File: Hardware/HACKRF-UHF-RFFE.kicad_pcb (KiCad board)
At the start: 4 copper layers, 84 parts, among them J1 SMA_Wurth_60312242114510, J2 SMA_Wurth_60312242114510, J3 SMA_Wurth_60312242114510, K1 HF3-53, Q1 SSM3K15AFU, U1 SPF5189Z, U2 RFPA3800, U3 SPF5189Z, U4 AS169-73, U5 SPF5189Z, U6 AS169-73, U7 AS169-73

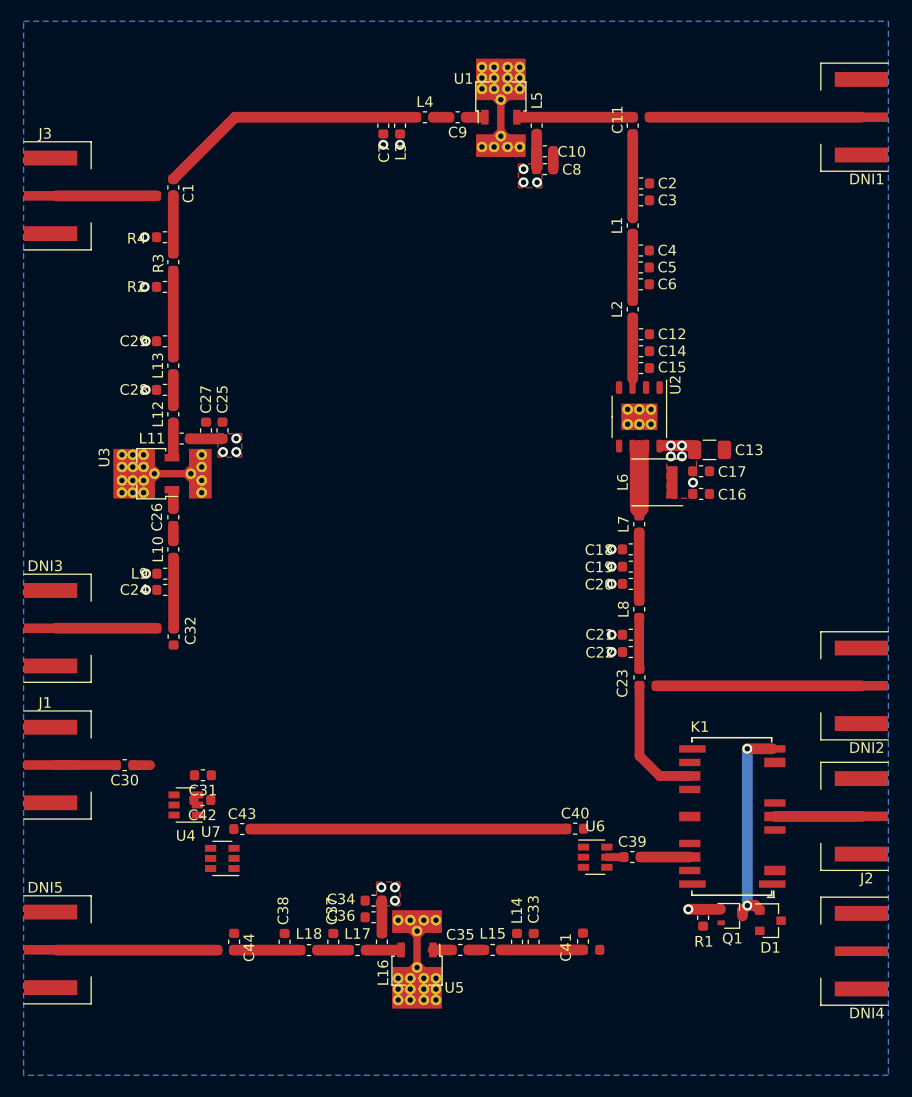
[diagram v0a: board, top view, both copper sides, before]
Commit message: Added discrete Chebyshev input filter to schematic based on Qucs simulationd. Artwork not done. It has occurred to me that I need to do some major cleanup of the test points on this PCBA.
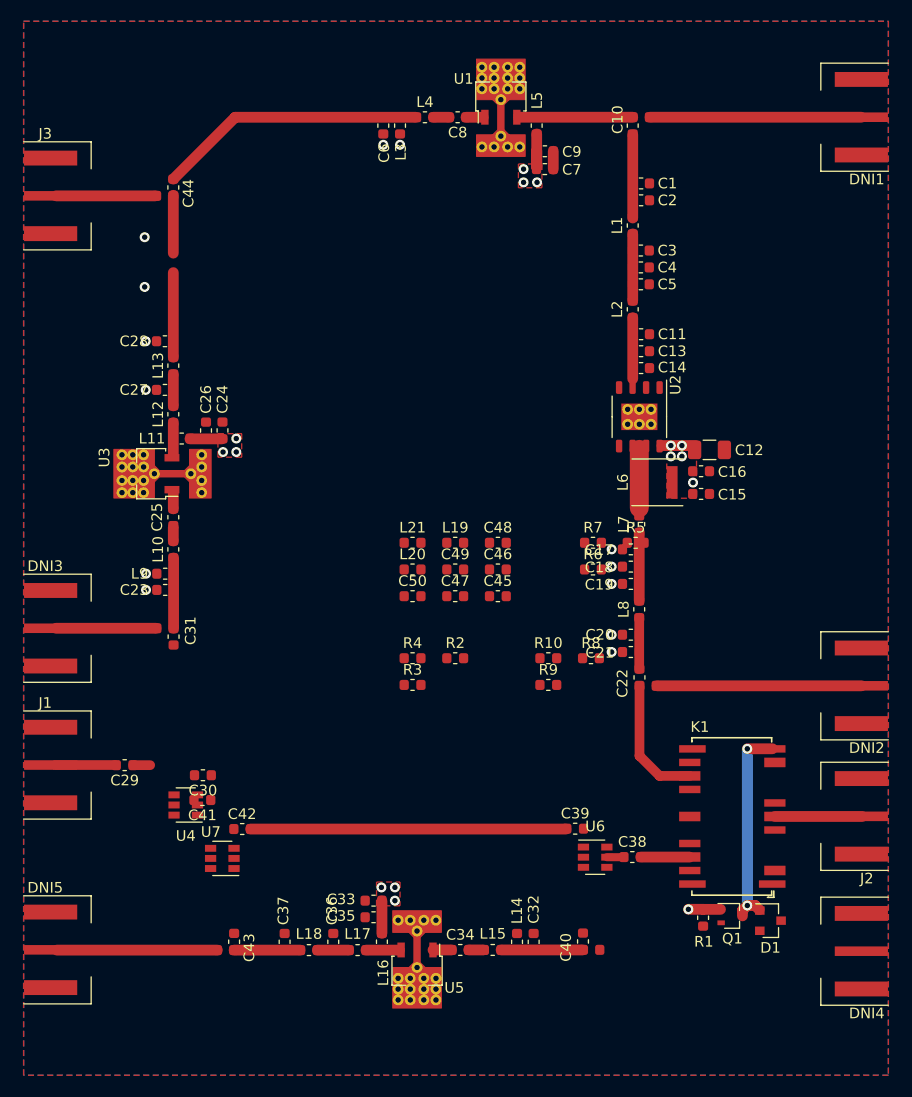
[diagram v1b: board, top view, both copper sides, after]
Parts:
- added C45: 600S100, Capacitor_SMD:C_0603_1608Metric, F.Cu at (143.6, 112.5)
- added C46: 600S220, Capacitor_SMD:C_0603_1608Metric, F.Cu at (143.6, 109.9)
- added C47: 600S2R7, Capacitor_SMD:C_0603_1608Metric, F.Cu at (139.6, 112.5)
- added C48: 600S2R7, Capacitor_SMD:C_0603_1608Metric, F.Cu at (143.6, 107.4)
- added C49: 600S220, Capacitor_SMD:C_0603_1608Metric, F.Cu at (139.6, 109.9)
- added C50: 600S100, Capacitor_SMD:C_0603_1608Metric, F.Cu at (135.6, 112.5)
- added L19: 0603HP-3N6X, Inductor_SMD:L_0603_1608Metric, F.Cu at (139.6, 107.4)
- added L20: 0603HP-82NX, Inductor_SMD:L_0603_1608Metric, F.Cu at (135.6, 109.9)
- added L21: 0603HP-3N6X, Inductor_SMD:L_0603_1608Metric, F.Cu at (135.6, 107.4)
- added R10: RT0603DRE0796R5L, Resistor_SMD:R_0603_1608Metric, F.Cu at (148.4, 118.3)
- added R5: RT0603DRE0796R5L, Resistor_SMD:R_0603_1608Metric, F.Cu at (156.6, 107.4)
- added R6: RT0603BRD0771R5L, Resistor_SMD:R_0603_1608Metric, F.Cu at (152.6, 109.9)
- added R7: RT0603DRE0796R5L, Resistor_SMD:R_0603_1608Metric, F.Cu at (152.6, 107.4)
- added R8: RT0603DRE0796R5L, Resistor_SMD:R_0603_1608Metric, F.Cu at (152.4, 118.3)
- added R9: RT0603BRD0771R5L, Resistor_SMD:R_0603_1608Metric, F.Cu at (148.4, 120.8)
- moved R4 45.9 mm to (135.6, 118.3), turned to 0 degrees
- moved R3 45.7 mm to (135.6, 120.8), turned to 0 degrees
- moved R2 44.3 mm to (139.6, 118.3), turned to 0 degrees
- renumbered C2 to C1, C11 to C10, C12 to C11, C13 to C12, C14 to C13, C15 to C14, C16 to C15, C17 to C16, C18 to C17, C19 to C18, C20 to C19, C3 to C2, C21 to C20, C22 to C21, C23 to C22, C24 to C23, C25 to C24, C26 to C25, C27 to C26, C28 to C27, C29 to C28, C30 to C29, C4 to C3, C31 to C30, C32 to C31, C33 to C32, C34 to C33, C35 to C34, C36 to C35, C37 to C36, C38 to C37, C39 to C38, C40 to C39, C5 to C4, C41 to C40, C42 to C41, C43 to C42, C44 to C43, C1 to C44, C6 to C5, C7 to C6, C8 to C7, C9 to C8, C10 to C9
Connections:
- J1 pad 1: /sheet5F20A948/J1 -> /Sheet5F20B395/RF_IN
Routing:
- added copper zone on F.Cu, net GNDA

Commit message: Major cleanup to both the schematic and directory structure. Stackup has changed accomodate to 0.65mm trace width. Chebyshev filter lived through the experience in the Qucs simulation; others not checked yet. I do want to re-visit the matching networks of all of the amplifiers as I have developed some good strategies to implement them.
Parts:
- removed J3: SMA_Wurth_60312242114510, RF:SMA_Wurth_60312242114510
- added C51: 600S101_3-pad-R, Capacitor_SMD:C_0603_1608Metric_3-pad-R, F.Cu at (-156.7, -74.0)
- added DNI6: SMA_Wurth_60312242114510, RF:SMA_Wurth_60312242114510, F.Cu at (-163.9, -69.6)
- C1: value 600S1R5 -> 600S101
- C10: value 600S101_3-pad-R -> 600S101; footprint Capacitor_SMD:C_0603_1608Metric_3-pad-R -> Capacitor_SMD:C_0603_1608Metric
- C11: value 600S3R3 -> 600S101
- C12: value T491A106M016AH -> 600S101_3-pad-L; footprint Capacitor_SMD:C_1206_3216Metric -> Capacitor_SMD:C_0603_1608Metric_3-pad-L
- C13, C2: value 600S100 -> 600S101
- C14: value 600S120 -> 600S101
- C15: value CC0603KRX7R9BB104 -> 600S101_3-pad-R; footprint Capacitor_SMD:C_0603_1608Metric -> Capacitor_SMD:C_0603_1608Metric_3-pad-R
- C16: value 600S101 -> 600S100; footprint Resistor_SMD:R_0603_1608Metric -> Capacitor_SMD:C_0603_1608Metric
- C17: value 600S270 -> 600S220
- C18: value 600S100 -> 600S2R7
- C19: value 600S3R6 -> 600S2R7
- C20: value 600S100 -> 600S220
- C21, C34: value 600S2R2 -> 600S100
- C22: value 600S101_3-pad-L -> 600S101; footprint Capacitor_SMD:C_0603_1608Metric_3-pad-L -> Capacitor_SMD:C_0603_1608Metric
- C23: value 600S120 -> 600S1R5
- C24: value CC0603KRX7R9BB104 -> 600S100
- C25: value 600S2R2 -> 600S3R0
- C26, C39, C41: value 600S101 -> 600S100
- C27: value 600S6R2 -> 600S270
- C28: value 600S5R1 -> 600S120; footprint Capacitor_SMD:C_0603_1608Metric -> Resistor_SMD:R_0603_1608Metric
- C29: value 600S101 -> CC0603KRX7R9BB104
- C3: value 600S3R0 -> 600S101_3-pad-L; footprint Capacitor_SMD:C_0603_1608Metric -> Capacitor_SMD:C_0603_1608Metric_3-pad-L
- C30: value 600S101 -> 600S2R2; footprint Capacitor_SMD:C_0603_1608Metric -> Resistor_SMD:R_0603_1608Metric
- C31: value 600S101_3-pad-L -> 600S101; footprint Capacitor_SMD:C_0603_1608Metric_3-pad-L -> Resistor_SMD:R_0603_1608Metric
- C32: value 600S120 -> 600S3R3
- C33: value CC0603KRX7R9BB104 -> T491A106M016AH; footprint Capacitor_SMD:C_0603_1608Metric -> Capacitor_SMD:C_1206_3216Metric
- C35: value 600S101 -> 600S120
- C36: value 600S6R2 -> CC0603KRX7R9BB104
- C37: value 600S5R1 -> 600S101; footprint Capacitor_SMD:C_0603_1608Metric -> Resistor_SMD:R_0603_1608Metric
- C38: value 600S101 -> 600S270
- C4, C45: value 600S100 -> 600S120
- C40: value 600S101_3-pad-L -> 600S3R6; footprint Capacitor_SMD:C_0603_1608Metric_3-pad-L -> Capacitor_SMD:C_0603_1608Metric
- C42: value 600S101 -> 600S2R2
- C44: value 600S101_3-pad-R -> 600S101_3-pad-L; footprint Capacitor_SMD:C_0603_1608Metric_3-pad-R -> Capacitor_SMD:C_0603_1608Metric_3-pad-L
- C46: value 600S220 -> CC0603KRX7R9BB104
- C47: value 600S2R7 -> 600S2R2
- C48: value 600S2R7 -> 600S101
- C49: value 600S220 -> 600S6R2
- C5: value 600S270 -> CC0603KRX7R9BB104
- C50: value 600S100 -> 600S5R1
- C6: value 600S120 -> 600S2R2; footprint Resistor_SMD:R_0603_1608Metric -> Capacitor_SMD:C_0603_1608Metric
- C7: value CC0603KRX7R9BB104 -> 600S101
- C8: value 600S2R2 -> 600S6R2; footprint Resistor_SMD:R_0603_1608Metric -> Capacitor_SMD:C_0603_1608Metric
- C9: value 600S101 -> 600S5R1; footprint Resistor_SMD:R_0603_1608Metric -> Capacitor_SMD:C_0603_1608Metric
- L1: footprint Inductor_SMD:L_0603_1608Metric -> Resistor_SMD:R_0603_1608Metric
- L10, L15: value 0603HP-51NX -> 0603HP-1N8X; footprint Resistor_SMD:R_0603_1608Metric -> Inductor_SMD:L_0603_1608Metric
- L11: value 0603HP-R22X -> 0603HP-8N2X
- L12: value 0603HP-3N6X -> 0603HP-51NX
- L13: value 0603HP-15NX -> 0603HP-R22X
- L14: value 0603HP-8N2X -> 1111SQ-47N; footprint Resistor_SMD:R_0603_1608Metric -> Inductor_SMD:L_Coilcraft_1111SQ-47N
- L16: value 0603HP-R22X -> 0603HP-8N2X; footprint Resistor_SMD:R_0603_1608Metric -> Inductor_SMD:L_0603_1608Metric
- L17: value 0603HP-3N6X -> 0603HP-8N2X
- L18: value 0603HP-15NX -> 0603HP-51NX
- L19: value 0603HP-3N6X -> 0603HP-R22X; footprint Inductor_SMD:L_0603_1608Metric -> Resistor_SMD:R_0603_1608Metric
- L2: value 0603HP-1N8X -> 0603HP-51NX; footprint Inductor_SMD:L_0603_1608Metric -> Resistor_SMD:R_0603_1608Metric
- L20: value 0603HP-82NX -> 0603HP-3N6X; footprint Inductor_SMD:L_0603_1608Metric -> Resistor_SMD:R_0603_1608Metric
- L21: value 0603HP-3N6X -> 0603HP-15NX; footprint Inductor_SMD:L_0603_1608Metric -> Resistor_SMD:R_0603_1608Metric
- L3: value 0603HP-8N2X -> 0603HP-R22X
- L4: value 0603HP-51NX -> 0603HP-3N6X
- L5: value 0603HP-R22X -> 0603HP-15NX
- L6: value 1111SQ-47N -> 0603HP-3N6X; footprint Inductor_SMD:L_Coilcraft_1111SQ-47N -> Inductor_SMD:L_0603_1608Metric
- L7: value 0603HP-1N8X -> 0603HP-82NX
- L8: value 0603HP-8N2X -> 0603HP-3N6X
- L9: footprint Resistor_SMD:R_0603_1608Metric -> Inductor_SMD:L_0603_1608Metric
- U1, U3: value SPF5189Z -> AS169-73; footprint RF:SOT-89-3_Qorvo_SPF5189z -> Package_TO_SOT_SMD:SOT-23-6
- U2: value RFPA3800 -> SPF5189Z; footprint RF:SOIC-8_Qorvo_RFPA3800 -> RF:SOT-89-3_Qorvo_SPF5189z
- U6: value AS169-73 -> RFPA3800; footprint Package_TO_SOT_SMD:SOT-23-6 -> RF:SOIC-8_Qorvo_RFPA3800
- U7: value AS169-73 -> SPF5189Z; footprint Package_TO_SOT_SMD:SOT-23-6 -> RF:SOT-89-3_Qorvo_SPF5189z
- moved D1 438.0 mm to (-202.8, -88.1)
- moved DNI4 437.3 mm to (-213.6, -49.3), turned to 0 degrees
- moved K1 433.7 mm to (-210.8, -82.1), turned to 0 degrees
- moved Q1 431.1 mm to (-198.3, -88.6)
- moved R1 430.8 mm to (-203.0, -84.6), turned to 0 degrees
- moved U6 418.4 mm to (-212.4, -67.2)
- moved C38 414.7 mm to (-208.6, -60.2)
- moved L14 414.0 mm to (-213.6, -61.1), turned to 0 degrees
- moved C40 412.6 mm to (-200.6, -69.2), turned to 0 degrees
- moved C39 405.9 mm to (-202.2, -65.9)
- moved C32 405.2 mm to (-200.6, -63.4), turned to 0 degrees
- moved C34 401.8 mm to (-204.6, -60.9)
- moved L8 400.6 mm to (-214.6, -36.1), turned to 0 degrees
- moved C18 399.3 mm to (-214.6, -38.6), turned to 0 degrees
- moved L15 399.3 mm to (-196.6, -64.1), turned to 0 degrees
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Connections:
- C1 pad 1: /Sheet5F04F5B5/PA_Driver/RF_OUT -> Net-(C1-Pad1)
- C1 pad 2: GNDA -> /sheet5F20A948/J1
- C10 pad 2: /Sheet5F04F5B5/PA_Driver/RF_OUT -> /sheet5F20DB04/J1
- C11 pad 1: /Sheet5F04F5B5/PA_Final/RF_IN -> /sheet5F2751CB/J2
- C11 pad 2: GNDA -> Net-(C11-Pad2)
- C12 pad 1: /Sheet5F04F5B5/P7V -> /sheet5F20DB04/J2
- C12 pad 2: GNDA -> /sheet5F20DB04/Sheet5F1AEEB0/DISCONNECT
- C13 pad 1: /Sheet5F04F5B5/PA_Final/RF_IN -> Net-(C13-Pad1)
- C13 pad 2: GNDA -> /sheet5F2751CB/J1
- C14 pad 1: /Sheet5F04F5B5/PA_Final/RF_IN -> /sheet5F2751CB/J2
- C14 pad 2: GNDA -> Net-(C14-Pad2)
- C15 pad 1: /Sheet5F04F5B5/P7V -> /sheet5F2751CB/J3
- C15 pad 2: GNDA -> /sheet5F2751CB/Sheet5F1B84EB/DISCONNECT
- C16 pad 1: /Sheet5F04F5B5/P7V -> /Sheet5F20B395/sheet5F216BC2/RF_IN
- C16 pad 2: GNDA -> GND
- C17 pad 1: Net-(C17-Pad1) -> /Sheet5F20B395/sheet5F216BC2/RF_IN
- C17 pad 2: GNDA -> GND
- C18 pad 1: Net-(C17-Pad1) -> Net-(C18-Pad1)
- C18 pad 2: GNDA -> /Sheet5F20B395/sheet5F216BC2/RF_IN
- C19 pad 1: Net-(C17-Pad1) -> Net-(C19-Pad1)
- C19 pad 2: GNDA -> /Sheet5F20B395/sheet5F20E71B/RF_IN
- C2 pad 1: /Sheet5F04F5B5/PA_Driver/RF_OUT -> /sheet5F2751CB/J1
- C2 pad 2: GNDA -> Net-(C2-Pad2)
- C20 pad 1: Net-(C20-Pad1) -> GND
- C20 pad 2: GNDA -> /Sheet5F20B395/sheet5F20E71B/RF_IN
- C21 pad 1: Net-(C20-Pad1) -> /Sheet5F20B395/sheet5F20E71B/RF_IN
- C21 pad 2: GNDA -> GND
- C22 pad 1: /Sheet5F04F5B5/RF_OUT -> /Sheet5F204DEB/sheet5F205D86/RF_IN
- C22 pad 2: Net-(C20-Pad1) -> /Sheet5F204DEB/sheet5F205D85/RF_OUT
- C23 pad 1: /sheet5F20A948/J2 -> /Sheet5F204DEB/sheet5F205D84/sheet5F1B5FB9/RF
- C23 pad 2: GNDA -> GND
- C24 pad 1: /Sheet5F042EDB/V_BIAS -> /Sheet5F204DEB/sheet5F205D84/sheet5F1B5FB9/RF
- C24 pad 2: GNDA -> GND
- C25 pad 2: Net-(C25-Pad2) -> GND
- C26 pad 1: /Sheet5F042EDB/V_BIAS -> Net-(C25-Pad1)
- C26 pad 2: GNDA -> GND
- C27 pad 1: Net-(C27-Pad1) -> Net-(C25-Pad1)
- C27 pad 2: GNDA -> GND
- C28 pad 1: /sheet5F19BA75/RF_IN -> /Sheet5F204DEB/sheet5F205D87/RF
- C28 pad 2: GNDA -> GND
- C29 pad 1: Net-(C29-Pad1) -> /P5V_Driver_2
- C29 pad 2: /sheet5F20A948/J1 -> GND
- C3 pad 1: Net-(C3-Pad1) -> /sheet5F20A948/J2
- C3 pad 2: GNDA -> /sheet5F20A948/Sheet5F1AEEB0/DISCONNECT
- C30 pad 1: /sheet5F2751CB/J1 -> Net-(C30-Pad1)
- C31 pad 1: /sheet5F20A948/J2 -> /P5V_Driver_2
- C31 pad 2: Net-(C31-Pad2) -> GND
- C32 pad 1: /sheet5F20DB04/J2 -> /Sheet5F204DEB/sheet5F205D84/PA_Final/RF_IN
- C32 pad 2: GNDA -> GND
- C33 pad 1: /sheet5F21A103/V_BIAS -> /P7V_Final
- C33 pad 2: GNDA -> GND
- C34 pad 1: Net-(C34-Pad1) -> /Sheet5F204DEB/sheet5F205D84/PA_Final/RF_IN
- C34 pad 2: Net-(C34-Pad2) -> GND
- C35 pad 1: /sheet5F21A103/V_BIAS -> /Sheet5F204DEB/sheet5F205D84/PA_Final/RF_IN
- C35 pad 2: GNDA -> GND
- C36 pad 1: Net-(C36-Pad1) -> /P7V_Final
- C36 pad 2: GNDA -> GND
- C37 pad 1: /sheet5F2751CB/J3 -> /P7V_Final
- C37 pad 2: GNDA -> GND
- C38 pad 2: /sheet5F20DB04/J1 -> GND
- C39 pad 1: /sheet5F2751CB/J2 -> Net-(C38-Pad1)
- C39 pad 2: Net-(C39-Pad2) -> GND
- C4 pad 1: Net-(C3-Pad1) -> /sheet5F20DB04/J2
- C4 pad 2: GNDA -> GND
- C40 pad 1: /sheet5F20DB04/J2 -> Net-(C38-Pad1)
- C40 pad 2: Net-(C40-Pad2) -> GND
- C41 pad 1: Net-(C41-Pad1) -> /Sheet5F204DEB/sheet5F205D84/sheet5F1BF908/RF
- C41 pad 2: /sheet5F2751CB/J1 -> GND
- C42 pad 1: /sheet5F2751CB/J2 -> /Sheet5F204DEB/sheet5F205D84/sheet5F1BF908/RF
- C42 pad 2: Net-(C42-Pad2) -> GND
- C43 pad 1: /sheet5F2751CB/J3 -> /Sheet5F204DEB/sheet5F205D84/sheet5F1B5FB9/RF
- C43 pad 2: Net-(C43-Pad2) -> /Sheet5F204DEB/sheet5F205D84/sheet5F1B5FB9/DISCONNECT
- C44 pad 1: Net-(C44-Pad1) -> /Sheet5F204DEB/sheet5F205D84/sheet5F1BF908/RF
- C44 pad 2: /Sheet5F04F5B5/RF_IN -> /Sheet5F204DEB/RF_OUT
- C45 pad 1: /Sheet5F20B395/sheet5F216BC2/RF_IN -> /sheet5F20A948/J2
- C45 pad 2: GNDA -> GND
- C46 pad 1: /Sheet5F20B395/sheet5F216BC2/RF_IN -> /P5V_Driver_1
- C46 pad 2: GNDA -> GND
- C47 pad 2: /Sheet5F20B395/sheet5F216BC2/RF_IN -> Net-(C47-Pad2)
- C48 pad 1: Net-(C48-Pad1) -> /P5V_Driver_1
- C48 pad 2: /Sheet5F20B395/sheet5F20E71B/RF_IN -> GND
- C49 pad 1: GNDA -> Net-(C49-Pad1)
- C49 pad 2: /Sheet5F20B395/sheet5F20E71B/RF_IN -> GND
- C5 pad 1: Net-(C3-Pad1) -> /sheet5F21A103/V_BIAS
- C5 pad 2: GNDA -> GND
- C50 pad 1: /Sheet5F20B395/sheet5F20E71B/RF_IN -> /Sheet5F204DEB/sheet5F205D85/RF_OUT
- C50 pad 2: GNDA -> GND
- C6 pad 1: /Sheet5F04F5B5/RF_IN -> Net-(C6-Pad1)
- C6 pad 2: GNDA -> Net-(C6-Pad2)
- C7 pad 1: /Sheet5F04F5B5/P5V -> /sheet5F21A103/V_BIAS
- C7 pad 2: GNDA -> GND
- C8 pad 2: Net-(C8-Pad2) -> GND
- C9 pad 1: /Sheet5F04F5B5/P5V -> /sheet5F2751CB/J3
- C9 pad 2: GNDA -> GND
- DNI1 pad 1: Net-(C10-Pad3) -> Net-(C3-Pad3)
- DNI1 pad 2: GNDA -> GND
- DNI2 pad 1: Net-(C22-Pad3) -> Net-(C12-Pad3)
- DNI2 pad 2: GNDA -> GND
- DNI3 pad 1: Net-(C31-Pad3) -> Net-(C15-Pad3)
- DNI3 pad 2: GNDA -> GND
- DNI4 pad 1: Net-(C40-Pad3) -> Net-(C43-Pad3)
- DNI4 pad 2: GNDA -> GND
- DNI5 pad 1: Net-(C43-Pad3) -> Net-(C44-Pad3)
- DNI5 pad 2: GNDA -> GND
- J1 pad 2: GNDA -> GND
- J2 pad 2: GNDA -> GND
- K1 pad 10: GNDA -> GND
- K1 pad 12: GNDA -> GND
- K1 pad 13: GNDA -> GND
- K1 pad 14: /Sheet5F04F5B5/RF_OUT -> /Sheet5F204DEB/RF_OUT
- K1 pad 15: GNDA -> GND
- K1 pad 17: GNDA -> GND
- K1 pad 19: GNDA -> GND
- K1 pad 2: GNDA -> GND
- K1 pad 21: GNDA -> GND
- K1 pad 22: GNDA -> GND
- K1 pad 5: GNDA -> GND
- K1 pad 7: GNDA -> GND
- L1 pad 1: /Sheet5F04F5B5/PA_Driver/RF_OUT -> /sheet5F20DB04/J2
- L1 pad 2: Net-(C3-Pad1) -> GND
- L10 pad 1: /sheet5F20A948/J2 -> Net-(C25-Pad1)
- L10 pad 2: Net-(C25-Pad2) -> /Sheet5F204DEB/sheet5F205D84/PA_Final/RF_IN
- L11 pad 1: /Sheet5F042EDB/V_BIAS -> /Sheet5F204DEB/sheet5F205D87/RF
- L11 pad 2: Net-(L11-Pad2) -> GND
- L12 pad 1: Net-(L11-Pad2) -> /Sheet5F204DEB/sheet5F205D87/RF
- L12 pad 2: Net-(C27-Pad1) -> Net-(C30-Pad2)
- L13 pad 1: Net-(C27-Pad1) -> /P5V_Driver_2
- L13 pad 2: /sheet5F19BA75/RF_IN -> /Sheet5F204DEB/sheet5F205D84/sheet5F1B5FB9/DISCONNECT
- L14 pad 1: /sheet5F20DB04/J2 -> /P7V_Final
- L14 pad 2: GNDA -> Net-(L14-Pad2)
- L15 pad 1: /sheet5F20DB04/J2 -> Net-(L14-Pad2)
- L15 pad 2: Net-(C34-Pad2) -> Net-(C38-Pad1)
- L16 pad 1: /sheet5F21A103/V_BIAS -> Net-(C38-Pad1)
- L16 pad 2: Net-(L16-Pad2) -> /Sheet5F204DEB/sheet5F205D84/sheet5F1BF908/RF
- L17 pad 1: Net-(L16-Pad2) -> /sheet5F20A948/J2
- L17 pad 2: Net-(C36-Pad1) -> GND
- L18 pad 1: Net-(C36-Pad1) -> /sheet5F20A948/J2
- L18 pad 2: /sheet5F2751CB/J3 -> Net-(C47-Pad2)
- L19 pad 1: GNDA -> /P5V_Driver_1
- L19 pad 2: /Sheet5F20B395/sheet5F216BC2/RF_IN -> Net-(L19-Pad2)
- L2 pad 1: Net-(C3-Pad1) -> /sheet5F20DB04/J2
- L2 pad 2: /Sheet5F04F5B5/PA_Final/RF_IN -> Net-(C6-Pad2)
- L20 pad 1: Net-(C47-Pad1) -> Net-(L19-Pad2)
- L20 pad 2: Net-(C48-Pad1) -> Net-(C49-Pad1)
- L21 pad 1: GNDA -> Net-(C49-Pad1)
- L21 pad 2: /Sheet5F20B395/sheet5F20E71B/RF_IN -> /Sheet5F204DEB/sheet5F205D85/RF_OUT
- L3 pad 1: /Sheet5F04F5B5/RF_IN -> /sheet5F21A103/V_BIAS
- L3 pad 2: GNDA -> Net-(L3-Pad2)
- L4 pad 1: /Sheet5F04F5B5/RF_IN -> Net-(L3-Pad2)
- L4 pad 2: Net-(C8-Pad2) -> Net-(C8-Pad1)
- L5 pad 1: /Sheet5F04F5B5/P5V -> Net-(C8-Pad1)
- L5 pad 2: Net-(C10-Pad1) -> /sheet5F2751CB/J3
- L6 pad 1: /Sheet5F04F5B5/P7V -> GND
- L6 pad 2: Net-(L6-Pad2) -> /Sheet5F20B395/sheet5F216BC2/RF_IN
- L7 pad 1: Net-(L6-Pad2) -> Net-(C18-Pad1)
- L7 pad 2: Net-(C17-Pad1) -> Net-(C19-Pad1)
- L8 pad 1: Net-(C17-Pad1) -> GND
- L8 pad 2: Net-(C20-Pad1) -> /Sheet5F20B395/sheet5F20E71B/RF_IN
- L9 pad 1: /sheet5F20A948/J2 -> /Sheet5F204DEB/sheet5F205D84/sheet5F1B5FB9/RF
- L9 pad 2: GNDA -> Net-(C25-Pad1)
- Q1 pad 2: GNDA -> GND
- R1 pad 2: GNDA -> GND
- R10 pad 1: /sheet5F20A948/J1 -> /Sheet5F204DEB/sheet5F205D87/DISCONNECT
- R10 pad 2: GNDA -> GND
- R2 pad 1: /sheet5F19BA75/RF_IN -> /Sheet5F20B395/RF_IN
- R2 pad 2: GNDA -> GND
- R3 pad 1: Net-(C44-Pad1) -> /Sheet5F20B395/sheet5F216BC2/RF_IN
- R3 pad 2: /sheet5F19BA75/RF_IN -> /Sheet5F20B395/RF_IN
- R4 pad 1: Net-(C44-Pad1) -> /Sheet5F20B395/sheet5F216BC2/RF_IN
- R4 pad 2: GNDA -> GND
- R5 pad 1: /Sheet5F20B395/RF_IN -> /Sheet5F20B395/sheet5F20E71B/RF_IN
- R5 pad 2: GNDA -> GND
- R6 pad 1: /Sheet5F20B395/sheet5F216BC2/RF_IN -> /sheet5F20A948/J1
- R6 pad 2: /Sheet5F20B395/RF_IN -> /Sheet5F20B395/sheet5F20E71B/RF_IN
- R7 pad 1: /Sheet5F20B395/sheet5F216BC2/RF_IN -> /sheet5F20A948/J1
- R7 pad 2: GNDA -> GND
- R8 pad 1: /Sheet5F20B395/sheet5F20E71B/RF_IN -> /Sheet5F204DEB/sheet5F205D86/RF_IN
- R8 pad 2: GNDA -> GND
- R9 pad 1: /sheet5F20A948/J1 -> /Sheet5F204DEB/sheet5F205D87/DISCONNECT
- R9 pad 2: /Sheet5F20B395/sheet5F20E71B/RF_IN -> /Sheet5F204DEB/sheet5F205D86/RF_IN
- U1 pad 1: Net-(C8-Pad1) -> Net-(C2-Pad2)
- U1 pad 2: GNDA -> GND
- U1 pad 3: Net-(C10-Pad1) -> /sheet5F20A948/Sheet5F1AEEB0/DISCONNECT
- U2 pad 1: (no net) -> Net-(C6-Pad1)
- U2 pad 2: (no net) -> GND
- U2 pad 3: /Sheet5F04F5B5/PA_Final/RF_IN -> Net-(L3-Pad2)
- U3 pad 1: Net-(C25-Pad1) -> Net-(C11-Pad2)
- U3 pad 2: GNDA -> GND
- U3 pad 3: Net-(L11-Pad2) -> /sheet5F20DB04/Sheet5F1AEEB0/DISCONNECT
- U4 pad 1: Net-(C30-Pad2) -> /sheet5F2751CB/Sheet5F1B84EB/DISCONNECT
- U4 pad 2: GNDA -> GND
- U4 pad 3: Net-(C31-Pad2) -> Net-(C14-Pad2)
- U4 pad 5: Net-(C29-Pad1) -> Net-(C13-Pad1)
- U5 pad 1: Net-(C34-Pad1) -> Net-(C30-Pad1)
- U5 pad 2: GNDA -> GND
- U5 pad 3: Net-(L16-Pad2) -> /Sheet5F204DEB/sheet5F205D84/sheet5F1B5FB9/DISCONNECT
- U6 pad 1: Net-(C39-Pad2) -> (no net)
- U6 pad 2: GNDA -> (no net)
- U6 pad 3: Net-(C40-Pad2) -> /Sheet5F204DEB/sheet5F205D84/PA_Final/RF_IN
- U6 pad 5: Net-(C38-Pad1) -> (no net)
- U6 pad 6: (no net) -> Net-(L14-Pad2)
- U7 pad 1: Net-(C43-Pad2) -> Net-(C47-Pad1)
- U7 pad 2: GNDA -> GND
- U7 pad 3: Net-(C42-Pad2) -> Net-(L19-Pad2)
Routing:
- net /sheet5F2751CB/J2: track 29.6 -> 0.00 mm
- net /Sheet5F04F5B5/RF_IN: track 25.2 -> 0.00 mm
- net Net-(C10-Pad3): track 19.9 -> 0.00 mm
- net Net-(D1-Pad1): track 19.5 -> 0.00 mm, vias 2 -> 0
- net Net-(C22-Pad3): track 19.2 -> 0.00 mm
- net Net-(C43-Pad3): track 15.1 -> 0.00 mm
- net /Sheet5F04F5B5/RF_OUT: track 12.1 -> 0.00 mm
- net Net-(C10-Pad1): track 10.7 -> 0.00 mm
- net Net-(C31-Pad3): track 9.40 -> 0.00 mm
- net Net-(C44-Pad3): track 9.35 -> 0.00 mm
- net /RF_Relay_TE_HF3-53/ANT: track 8.22 -> 0.00 mm
- net /sheet5F19BA75/RF_IN: track 7.96 -> 0.00 mm
- net /Sheet5F04F5B5/PA_Driver/RF_OUT: track 7.82 -> 0.00 mm
- net /sheet5F20DB04/J2: track 7.66 -> 0.00 mm
- net /sheet5F20A948/J2: track 6.60 -> 0.00 mm
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- removed copper zone on F.Cu, net /Sheet5F042EDB/V_BIAS
- removed copper zone on F.Cu, net /Sheet5F04F5B5/P5V
- removed copper zone on F.Cu, net /Sheet5F04F5B5/P7V
- removed copper zone on F.Cu, net /sheet5F21A103/V_BIAS
- removed copper zone on B.Cu, net GNDA
- removed copper zone on C2, net GNDA
- removed copper zone on C3, net GNDA
- removed copper zone on F.Cu, net GNDA

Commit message: Improving LNA simulations and Documentation package. More to come on this one.
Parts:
- removed C1, C10, C11, C13, C14, C2, C22, C48, C7: 600S101, Capacitor_SMD:C_0603_1608Metric
- removed C12, C3, C44: 600S101_3-pad-L, Capacitor_SMD:C_0603_1608Metric_3-pad-L
- removed C15, C43, C51: 600S101_3-pad-R, Capacitor_SMD:C_0603_1608Metric_3-pad-R
- removed C16, C21, C24, C26, C34, C39, C41: 600S100, Capacitor_SMD:C_0603_1608Metric
- removed C17, C20: 600S220, Capacitor_SMD:C_0603_1608Metric
- removed C18, C19: 600S2R7, Capacitor_SMD:C_0603_1608Metric
- removed C23: 600S1R5, Capacitor_SMD:C_0603_1608Metric
- removed C25: 600S3R0, Capacitor_SMD:C_0603_1608Metric
- removed C27, C38: 600S270, Capacitor_SMD:C_0603_1608Metric
- removed C28: 600S120, Resistor_SMD:R_0603_1608Metric
- removed C29, C36, C46, C5: CC0603KRX7R9BB104, Capacitor_SMD:C_0603_1608Metric
- removed C30: 600S2R2, Resistor_SMD:R_0603_1608Metric
- removed C31, C37: 600S101, Resistor_SMD:R_0603_1608Metric
- removed C32: 600S3R3, Capacitor_SMD:C_0603_1608Metric
- removed C33: T491A106M016AH, Capacitor_SMD:C_1206_3216Metric
- removed C35, C4, C45: 600S120, Capacitor_SMD:C_0603_1608Metric
- removed C40: 600S3R6, Capacitor_SMD:C_0603_1608Metric
- removed C42, C47, C6: 600S2R2, Capacitor_SMD:C_0603_1608Metric
- removed C49, C8: 600S6R2, Capacitor_SMD:C_0603_1608Metric
- removed C50, C9: 600S5R1, Capacitor_SMD:C_0603_1608Metric
- removed D1: BAS21, Package_TO_SOT_SMD:SOT-23
- removed DNI1, DNI2, DNI3, DNI4, DNI5, DNI6, J1, J2: SMA_Wurth_60312242114510, RF:SMA_Wurth_60312242114510
- removed K1: HF3-53, Relay_SMD:Relay_SPDT_AXICOM_HF3Series_50ohms_Pitch1.27mm
- removed L1, L11, L17: 0603HP-8N2X, Resistor_SMD:R_0603_1608Metric
- removed L10, L15: 0603HP-1N8X, Inductor_SMD:L_0603_1608Metric
- removed L12, L18, L2: 0603HP-51NX, Resistor_SMD:R_0603_1608Metric
- removed L13, L19, L3: 0603HP-R22X, Resistor_SMD:R_0603_1608Metric
- removed L14: 1111SQ-47N, Inductor_SMD:L_Coilcraft_1111SQ-47N
- removed L16, L9: 0603HP-8N2X, Inductor_SMD:L_0603_1608Metric
- removed L20, L4: 0603HP-3N6X, Resistor_SMD:R_0603_1608Metric
- removed L21, L5: 0603HP-15NX, Resistor_SMD:R_0603_1608Metric
- removed L6, L8: 0603HP-3N6X, Inductor_SMD:L_0603_1608Metric
- removed L7: 0603HP-82NX, Inductor_SMD:L_0603_1608Metric
- removed Q1: SSM3K15AFU, Package_TO_SOT_SMD:SOT-323_SC-70
- removed R1: RT0603FRE0710KL, Resistor_SMD:R_0603_1608Metric
- removed R10, R2, R4, R5, R7, R8: RT0603DRE0796R5L, Resistor_SMD:R_0603_1608Metric
- removed R3, R6, R9: RT0603BRD0771R5L, Resistor_SMD:R_0603_1608Metric
- removed U1, U3, U4: AS169-73, Package_TO_SOT_SMD:SOT-23-6
- removed U2, U5, U7: SPF5189Z, RF:SOT-89-3_Qorvo_SPF5189z
- removed U6: RFPA3800, RF:SOIC-8_Qorvo_RFPA3800
